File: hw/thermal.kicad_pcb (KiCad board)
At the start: 2 copper layers, 110 x 60 mm, 40 parts, among them IC1 ATTINY2313-P, J1 USB_2, J2 RJ12, J3 DB9, J4 JACK_2P, Q1 IRL530N, Q2 IRL530N, U1 LM7805, U2 LTV847, X1 12MHz

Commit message: V2 hardware schematics and pcb
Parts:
- Q1, Q2: footprint TO220_VERT -> TO220GDS
- moved R15 14.1 mm to (160.0, 124.5)
- moved R13 8.98 mm to (156.2, 113.7)
- moved R16 2.62 mm to (154.9, 94.0), turned to 0 degrees
- moved R14 0.90 mm to (146.7, 101.6)
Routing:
- net +12V: track 45.1 -> 136.8 mm, vias 0 -> 2
- net GND: track 216.5 -> 267.6 mm, vias 0 -> 2
- net /TEMP2: track 3.81 -> 37.2 mm
- net /TEMP3: track 3.81 -> 36.6 mm
- net VCC: track 104.8 -> 136.3 mm, vias 0 -> 2
- net /TEMP1: track 8.30 -> 38.2 mm
- net /TEMP4: track 6.99 -> 36.5 mm
- net N-0000024: track 0.00 -> 22.5 mm
- net N-0000023: track 0.00 -> 9.99 mm
- net /FAN1: track 12.2 -> 20.6 mm
- net /FAN2: track 12.2 -> 11.3 mm

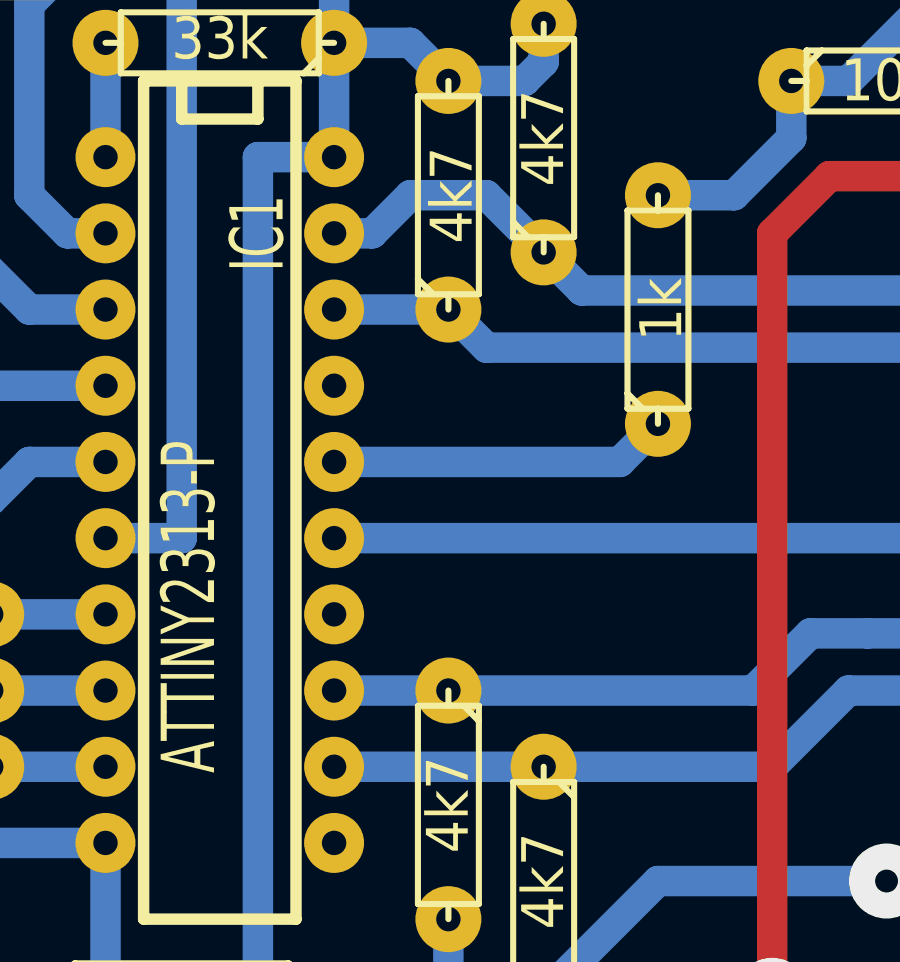
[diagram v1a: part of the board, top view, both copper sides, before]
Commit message: New INDI driver
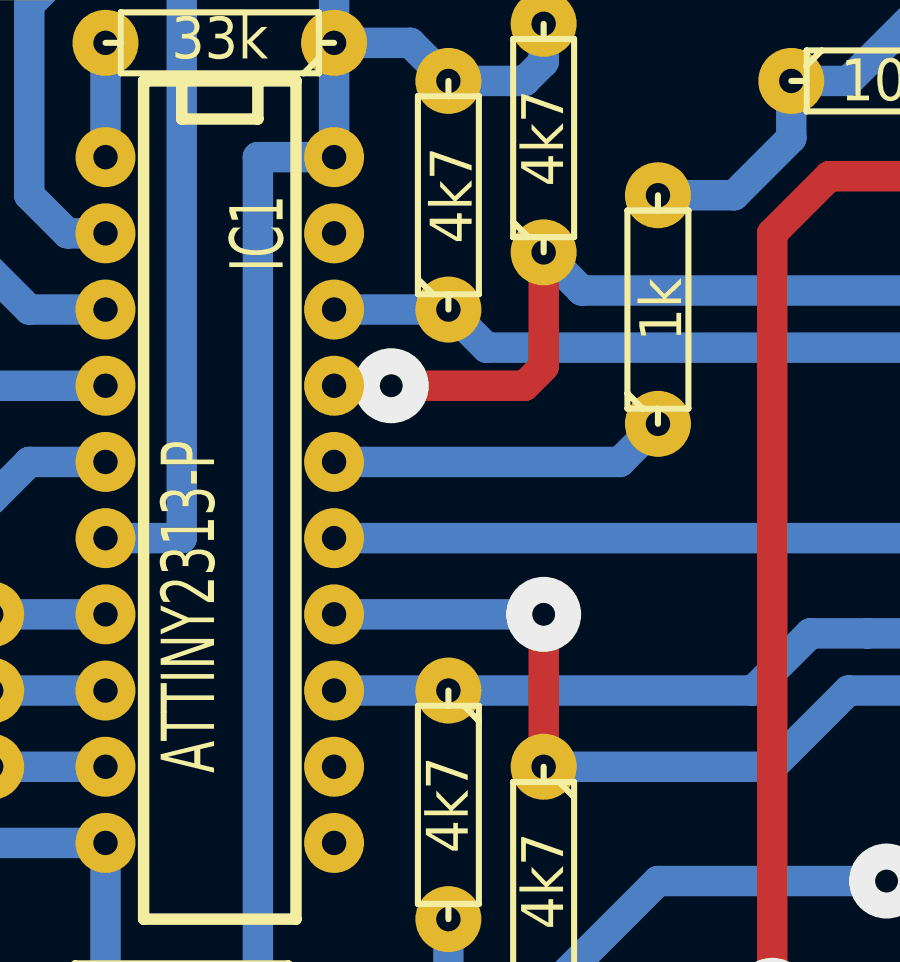
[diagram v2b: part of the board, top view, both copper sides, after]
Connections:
- IC1 pad 12: /TEMP4 -> (no net)
- IC1 pad 14: (no net) -> /TEMP4
- IC1 pad 17: (no net) -> /TEMP1
- IC1 pad 19: /TEMP1 -> (no net)
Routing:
- net /TEMP4: track 36.5 -> 41.6 mm, vias 0 -> 1
- net /TEMP1: track 38.2 -> 42.2 mm, vias 0 -> 1
